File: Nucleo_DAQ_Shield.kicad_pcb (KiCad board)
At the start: 2 copper layers, 53.3 x 78.1 mm, 34 parts, among them J1 CONN_01X05, J2 CONN_01X06, J3 CONN_01X02, J5 CONN_01X06, J6 CONN_COAXIAL, J8 CONN_02X04, J9 CONN_01X04, U1 4050, U10 ST_Nucleo144_F746ZG_CN10, U2 TL072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

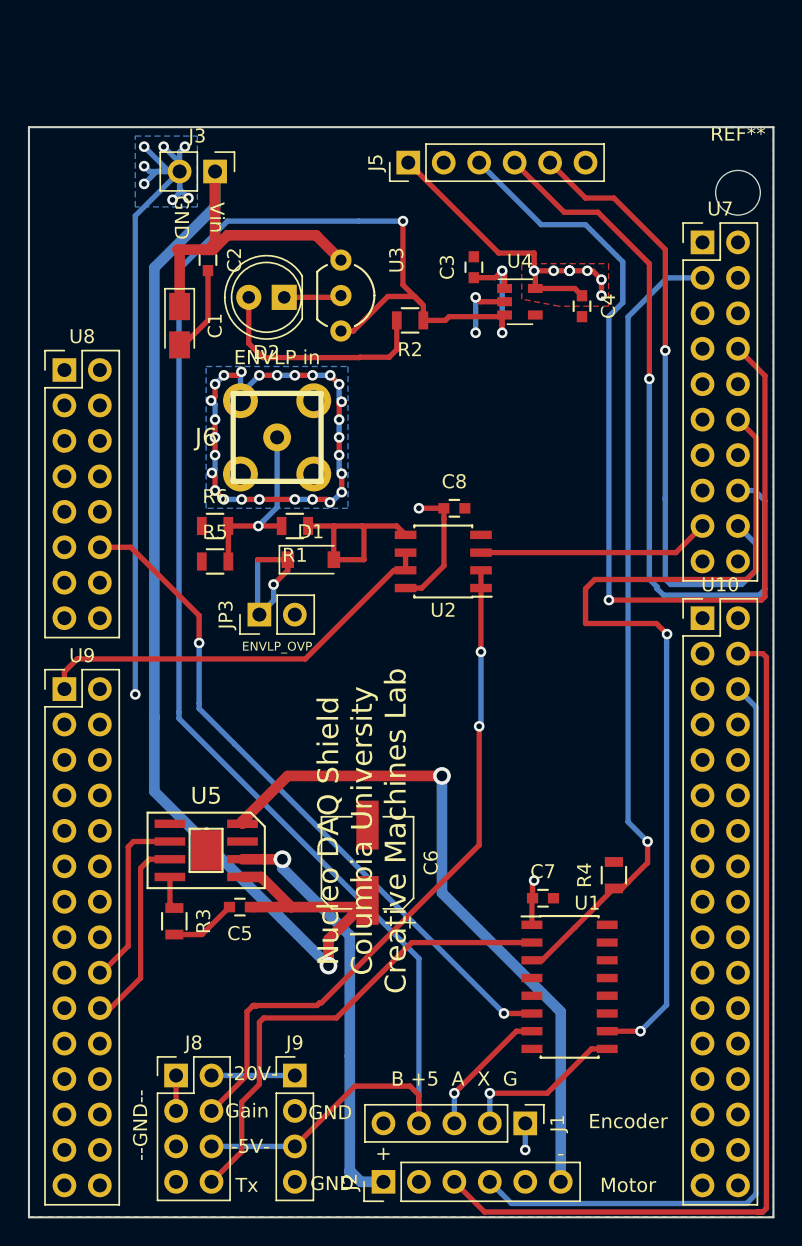
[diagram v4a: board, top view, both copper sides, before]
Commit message: Q2 footprint change, connect ground plane
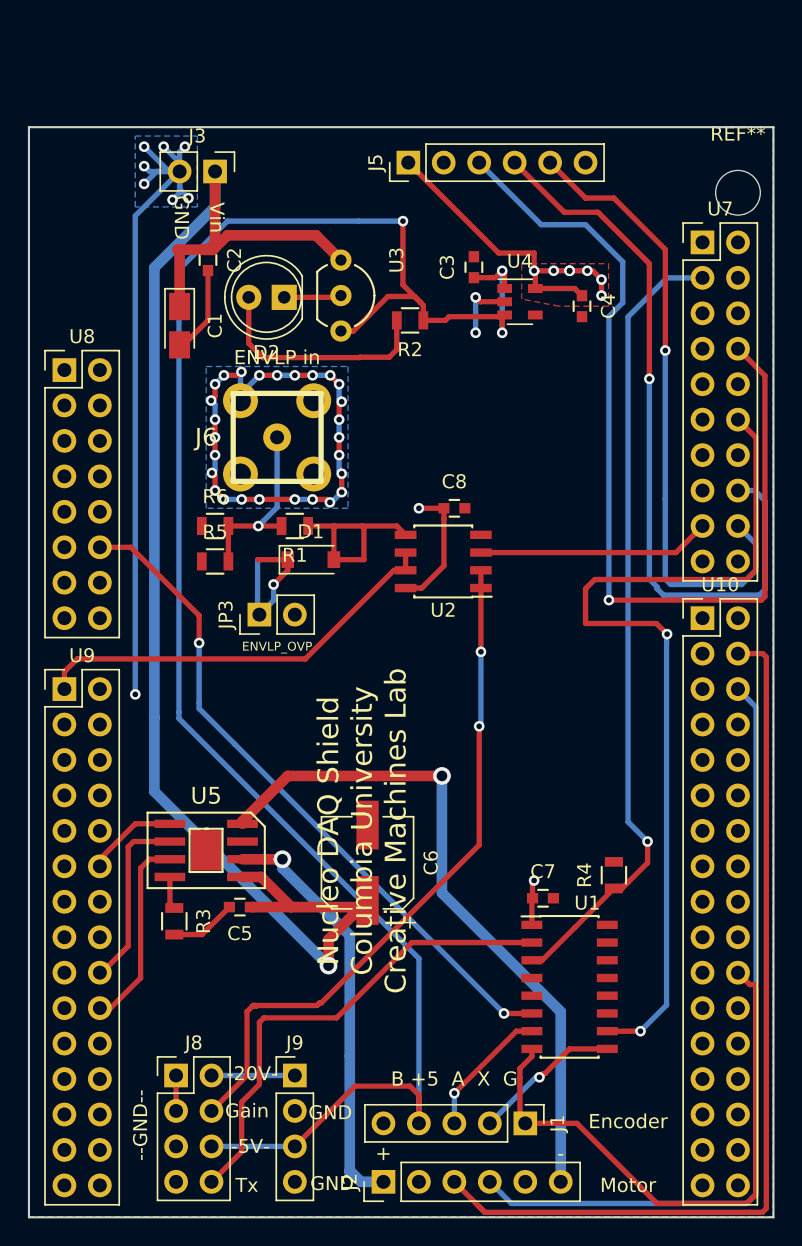
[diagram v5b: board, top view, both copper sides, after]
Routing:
- net GND: track 187.1 -> 233.2 mm, vias 39 -> 38
- net /5V_CUI_X: track 11.6 -> 10.6 mm
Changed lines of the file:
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@@
   (general
     (links 91)
-    (no_connects 3)
-    (area 140.894999 48.819999 194.385001 127.075001)
+    (no_connects 0)
+    (area 133.708523 46.220666 244.462898 129.674333)
     (thickness 1.6)
     (drawings 38)
-    (tracks 403)
+    (tracks 428)
     (zones 0)
     (modules 34)
@@
   (segment (start 151.626 57.67) (end 151.765 57.809) (width 0.762) (layer F.Cu) (net 1))
   (segment (start 151.765 57.809) (end 151.765 61.744) (width 0.762) (layer F.Cu) (net 1))
+  (segment (start 176.53 120.269) (end 180.228859 120.269) (width 0.381) (layer F.Cu) (net 2))
+  (segment (start 185.960431 126.008509) (end 185.960431 126.000571) (width 0.381) (layer F.Cu) (net 2))
+  (segment (start 185.960431 126.000572) (end 185.960431 126.008509) (width 0.381) (layer F.Cu) (net 2))
+  (segment (start 180.228859 120.269) (end 185.960431 126.000572) (width 0.381) (layer F.Cu) (net 2))
+  (segment (start 185.952501 126.008501) (end 185.960431 126.000571) (width 0.381) (layer F.Cu) (net 2))
+  (segment (start 192.619999 110.323999) (end 193.000999 110.323999) (width 0.381) (layer F.Cu) (net 2))
+  (segment (start 191.77 109.474) (end 192.619999 110.323999) (width 0.381) (layer F.Cu) (net 2))
+  (segment (start 193.064501 110.387501) (end 193.064501 125.451499) (width 0.381) (layer F.Cu) (net 2))
+  (segment (start 193.000999 110.323999) (end 193.064501 110.387501) (width 0.381) (layer F.Cu) (net 2))
+  (segment (start 192.391361 126.008501) (end 185.952501 126.008501) (width 0.381) (layer F.Cu) (net 2))
+  (segment (start 192.948363 125.451499) (end 192.391361 126.008501) (width 0.381) (layer F.Cu) (net 2))
+  (segment (start 193.064501 125.451499) (end 192.948363 125.451499) (width 0.381) (layer F.Cu) (net 2))
+  (segment (start 176.149 116.967) (end 176.149 119.888) (width 0.381) (layer F.Cu) (net 2))
+  (segment (start 176.149 119.888) (end 176.53 120.269) (width 0.381) (layer F.Cu) (net 2))
+  (segment (start 177.005 114.935) (end 177.005 115.476) (width 0.381) (layer F.Cu) (net 2))
+  (segment (start 176.149 116.332) (end 176.149 116.967) (width 0.381) (layer F.Cu) (net 2))
+  (segment (start 177.005 115.476) (end 176.149 116.332) (width 0.381) (layer F.Cu) (net 2))
+  (segment (start 146.05 101.854) (end 146.05 101.346) (width 0.381) (layer F.Cu) (net 2))
+  (segment (start 146.05 101.346) (end 148.59 98.806) (width 0.381) (layer F.Cu) (net 2))
+  (segment (start 148.59 98.806) (end 151.07 98.806) (width 0.381) (layer F.Cu) (net 2))
   (segment (start 182.523501 82.779499) (end 182.523501 62.459499) (width 0.381) (layer B.Cu) (net 2))
   (segment (start 193.699511 66.699511) (end 193.699511 82.525489) (width 0.381) (layer F.Cu) (net 2))
@@
   (via (at 172.974 61.087) (size 0.762) (drill 0.4) (layers F.Cu B.Cu) (net 2))
   (segment (start 173.289 61.402) (end 172.974 61.087) (width 0.381) (layer F.Cu) (net 2))
-  (segment (start 176.53 120.015) (end 176.53 122.174) (width 0.381) (layer B.Cu) (net 2))
-  (via (at 176.53 122.174) (size 0.762) (drill 0.4) (layers F.Cu B.Cu) (net 2))
   (segment (start 154.051 121.92) (end 160.02 121.92) (width 0.381) (layer B.Cu) (net 3))
   (segment (start 164.338 117.602) (end 160.02 121.92) (width 0.381) (layer F.Cu) (net 3))
@@
   (segment (start 171.45 118.11) (end 171.45 120.015) (width 0.381) (layer B.Cu) (net 100))
   (via (at 171.45 118.11) (size 0.762) (drill 0.4) (layers F.Cu B.Cu) (net 100))
-  (segment (start 173.99 118.11) (end 173.99 120.015) (width 0.381) (layer B.Cu) (net 101))
-  (via (at 173.99 118.11) (size 0.762) (drill 0.4) (layers F.Cu B.Cu) (net 101))
-  (segment (start 182.405 114.935) (end 181.274 114.935) (width 0.381) (layer F.Cu) (net 101))
-  (segment (start 181.274 114.935) (end 178.099 118.11) (width 0.381) (layer F.Cu) (net 101))
-  (segment (start 178.099 118.11) (end 173.99 118.11) (width 0.381) (layer F.Cu) (net 101))
+  (segment (start 177.546 116.967) (end 177.292 116.967) (width 0.381) (layer B.Cu) (net 101))
+  (segment (start 177.8 116.713) (end 177.546 116.967) (width 0.381) (layer F.Cu) (net 101))
+  (via (at 177.546 116.967) (size 0.762) (drill 0.4) (layers F.Cu B.Cu) (net 101))
+  (segment (start 182.405 114.935) (end 179.705 114.935) (width 0.381) (layer F.Cu) (net 101))
+  (segment (start 179.705 114.935) (end 177.927 116.713) (width 0.381) (layer F.Cu) (net 101))
+  (segment (start 177.927 116.713) (end 177.8 116.713) (width 0.381) (layer F.Cu) (net 101))
+  (segment (start 177.292 116.967) (end 173.99 120.269) (width 0.381) (layer B.Cu) (net 101))
   (segment (start 154.051 116.84) (end 160.02 116.84) (width 0.381) (layer B.Cu) (net 106))
   (segment (start 185.42 66.929) (end 185.42 58.674) (width 0.381) (layer F.Cu) (net 108))
@@
   (segment (start 186.563 81.28) (end 186.563 75.565) (width 0.381) (layer B.Cu) (net 109))
   (segment (start 186.563 75.565) (end 186.563 75.438) (width 0.381) (layer B.Cu) (net 109))
-  (segment (start 193.548 126.619) (end 193.167 126.619) (width 0.381) (layer F.Cu) (net 110))
+  (segment (start 192.659 126.643511) (end 193.523489 126.643511) (width 0.381) (layer F.Cu) (net 110))
+  (segment (start 193.523489 126.643511) (end 193.802 126.365) (width 0.381) (layer F.Cu) (net 110))
+  (segment (start 192.278 126.643511) (end 192.659 126.643511) (width 0.381) (layer F.Cu) (net 110))
+  (segment (start 192.278 126.643511) (end 173.633511 126.643511) (width 0.381) (layer F.Cu) (net 110))
+  (segment (start 193.548 86.614) (end 193.802 86.868) (width 0.381) (layer F.Cu) (net 110))
   (segment (start 191.77 86.614) (end 193.548 86.614) (width 0.381) (layer F.Cu) (net 110))
-  (segment (start 193.548 86.614) (end 193.802 86.868) (width 0.381) (layer F.Cu) (net 110))
-  (segment (start 193.802 86.868) (end 193.802 126.365) (width 0.381) (layer F.Cu) (net 110))
-  (segment (start 193.802 126.365) (end 193.548 126.619) (width 0.381) (layer F.Cu) (net 110))
-  (segment (start 193.548 126.619) (end 173.609 126.619) (width 0.381) (layer F.Cu) (net 110))
-  (segment (start 173.609 126.619) (end 171.45 124.46) (width 0.381) (layer F.Cu) (net 110))
+  (segment (start 193.802 125.857) (end 193.802 126.365) (width 0.381) (layer F.Cu) (net 110))
+  (segment (start 193.802 86.868) (end 193.802 125.857) (width 0.381) (layer F.Cu) (net 110))
+  (segment (start 173.633511 126.643511) (end 173.355 126.365) (width 0.381) (layer F.Cu) (net 110))
+  (segment (start 173.355 126.365) (end 173.228 126.238) (width 0.381) (layer F.Cu) (net 110))
+  (segment (start 173.609 126.619) (end 173.228 126.238) (width 0.381) (layer F.Cu) (net 110))
+  (segment (start 173.228 126.238) (end 171.45 124.46) (width 0.381) (layer F.Cu) (net 110))
   (segment (start 191.77 89.154) (end 193.064501 90.448501) (width 0.381) (layer B.Cu) (net 111))
   (segment (start 193.064501 90.448501) (end 193.064501 125.335361) (width 0.381) (layer B.Cu) (net 111))

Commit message: Necleo board encoder switch
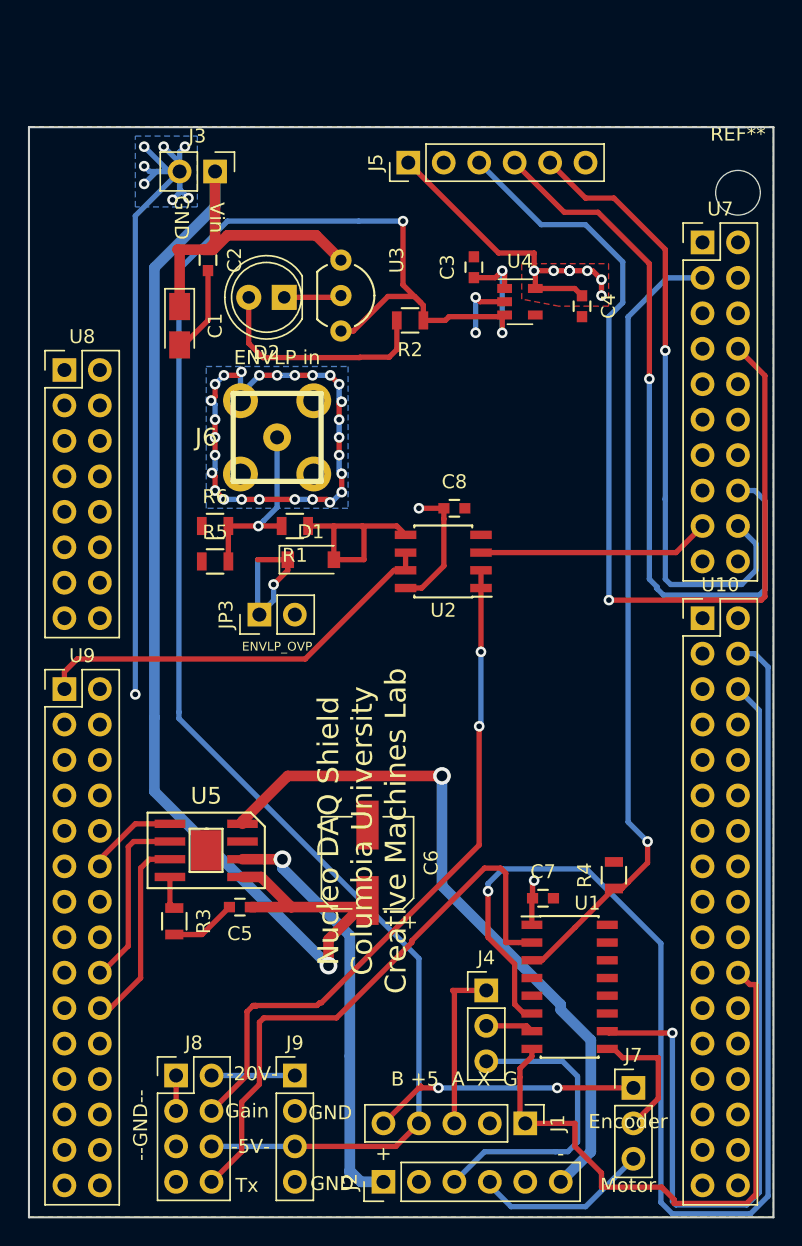
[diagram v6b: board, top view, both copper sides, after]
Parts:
- added J4: CONN_01X03, Pin_Headers:Pin_Header_Straight_1x03_Pitch2.54mm, F.Cu at (173.7, 110.7)
- added J7: CONN_01X03, Pin_Headers:Pin_Header_Straight_1x03_Pitch2.54mm, F.Cu at (184.3, 117.7)
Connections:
- J1 pad 2: /5V_CUI_X -> Net-(J1-Pad2)
- J1 pad 3: /5V_CUI_A -> /CUI_ENCODER_A
- J1 pad 5: Net-(J1-Pad5) -> /CUI_ENCODER_B
- J2 pad 3: /ENCODERA -> /MOT_ENCODER_A
- J2 pad 4: /ENCODERB -> /MOT_ENCODER_B
- U1 pad 10: /ENCODER_X -> /ENCODER_B_BUFFERED
- U1 pad 6: /ENCODER_A -> /ENCODER_A_BUFFERED
- U1 pad 7: /5V_CUI_A -> /ENCODER_A
- U1 pad 9: /5V_CUI_X -> /ENCODER_B
- U10 pad 4: /ENCODERA -> /ENCODER_A_BUFFERED
- U10 pad 6: /ENCODERB -> /ENCODER_B_BUFFERED
- U7 pad 12: /ENCODER_X -> Net-(U7-Pad12)
- U8 pad 12: /ENCODER_A -> Net-(U8-Pad12)
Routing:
- net /ENCODER_A_BUFFERED: track 0.00 -> 93.5 mm, vias 0 -> 1
- net /ENCODERA: track 65.5 -> 0.00 mm
- net /ENCODER_X: track 64.4 -> 0.00 mm, vias 2 -> 0
- net /ENCODER_B_BUFFERED: track 0.00 -> 60.2 mm, vias 0 -> 1
- net /ENCODERB: track 56.7 -> 0.00 mm
- net /ENCODER_A: track 48.7 -> 3.90 mm, vias 2 -> 0
- net /MOT_ENCODER_A: track 0.00 -> 21.7 mm
- net /CUI_ENCODER_B: track 0.00 -> 19.4 mm, vias 0 -> 2
- net /MOT_ENCODER_B: track 0.00 -> 12.6 mm
- net /CUI_ENCODER_A: track 0.00 -> 12.0 mm
- net /5V_CUI_X: track 10.6 -> 0.00 mm, vias 1 -> 0
- net /5V_CUI_A: track 9.78 -> 0.00 mm, vias 1 -> 0
- net /ENCODER_B: track 0.00 -> 9.35 mm
- net /Tx_Pulse_buffered: track 34.7 -> 42.1 mm
- net +5V: track 134.1 -> 131.0 mm
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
